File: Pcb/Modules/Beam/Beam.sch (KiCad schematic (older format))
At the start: 9 parts, among them J1 JACK_RJ45, Q1 Q_NMOS_GSD, U3 TSOP585xx

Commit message: Pcb layout for beam and projectile module
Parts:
- added C3: 10uF, Resistors_SMD:R_1206, symbol C_Small
- D1: value LD274 -> IR_LED; footprint LEDs:LED_D5.0mm -> LEDs:LED_D5.0mm_Horizontal_O1.27mm_Z15.0mm; symbol LD274 -> LED
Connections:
- net +3V3: now also C3.1
- net GND: now also C3.2
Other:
- moved on the sheet: C1
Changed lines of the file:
@@
 $EndDescr
 $Comp
-L LD274 D1
+L LED D1
 U 1 1 59CD43E5
-P 5450 2500
-F 0 "D1" H 5470 2570 50  0000 L CNN
-F 1 "LD274" H 5410 2390 50  0000 C CNN
-F 2 "LEDs:LED_D5.0mm" H 5450 2675 50  0001 C CNN
-F 3 "" H 5400 2500 50  0001 C CNN
-	1    5450 2500
+P 5450 2550
+F 0 "D1" H 5400 2650 50  0000 L CNN
+F 1 "IR_LED" H 5450 2400 50  0000 C CNN
+F 2 "LEDs:LED_D5.0mm_Horizontal_O1.27mm_Z15.0mm" H 5450 2725 50  0001 C CNN
+F 3 "" H 5400 2550 50  0001 C CNN
+	1    5450 2550
 	0    -1   -1   0
 $EndComp
@@
 L C_Small C1
 U 1 1 59D0EC2E
-P 3950 3450
-F 0 "C1" H 3960 3520 50  0000 L CNN
-F 1 "0.1uF" H 3960 3370 50  0000 L CNN
-F 2 "Resistors_SMD:R_0603" H 3950 3450 50  0001 C CNN
-F 3 "" H 3950 3450 50  0001 C CNN
-	1    3950 3450
-	1    0    0    -1
-$EndComp
-$Comp
-L +3.3V #PWR01
+P 3550 3450
+F 0 "C1" H 3560 3520 50  0000 L CNN
+F 1 "0.1uF" H 3560 3370 50  0000 L CNN
+F 2 "Resistors_SMD:R_0603" H 3550 3450 50  0001 C CNN
+F 3 "" H 3550 3450 50  0001 C CNN
+	1    3550 3450
+	1    0    0    -1
+$EndComp
+$Comp
+L +3.3V #PWR5
 U 1 1 59FCE3A1
 P 4500 2050
-F 0 "#PWR01" H 4500 1900 50  0001 C CNN
+F 0 "#PWR5" H 4500 1900 50  0001 C CNN
 F 1 "+3.3V" H 4500 2190 50  0000 C CNN
 F 2 "" H 4500 2050 50  0000 C CNN
@@
 $EndComp
 $Comp
-L GND #PWR02
+L GND #PWR6
 U 1 1 59FCE5A5
 P 4500 2850
-F 0 "#PWR02" H 4500 2600 50  0001 C CNN
+F 0 "#PWR6" H 4500 2600 50  0001 C CNN
 F 1 "GND" H 4500 2700 50  0000 C CNN
 F 2 "" H 4500 2850 50  0000 C CNN
@@
 $EndComp
 $Comp
-L GND #PWR03
+L GND #PWR10
 U 1 1 59FD6B4A
 P 6100 2100
-F 0 "#PWR03" H 6100 1850 50  0001 C CNN
+F 0 "#PWR10" H 6100 1850 50  0001 C CNN
 F 1 "GND" H 6100 1950 50  0000 C CNN
 F 2 "" H 6100 2100 50  0000 C CNN
@@
 $EndComp
 $Comp
-L +3.3V #PWR04
+L +3.3V #PWR9
 U 1 1 59FD6C0D
 P 5550 1300
-F 0 "#PWR04" H 5550 1150 50  0001 C CNN
+F 0 "#PWR9" H 5550 1150 50  0001 C CNN
 F 1 "+3.3V" H 5550 1440 50  0000 C CNN
 F 2 "" H 5550 1300 50  0000 C CNN
@@
 	6100 2000 6100 2100
 $Comp
-L GND #PWR05
+L GND #PWR11
 U 1 1 59FD6E29
 P 6450 2100
-F 0 "#PWR05" H 6450 1850 50  0001 C CNN
+F 0 "#PWR11" H 6450 1850 50  0001 C CNN
 F 1 "GND" H 6450 1950 50  0000 C CNN
 F 2 "" H 6450 2100 50  0000 C CNN
@@
 	6450 1850 6450 2100
 $Comp
-L GND #PWR06
+L GND #PWR2
 U 1 1 59FD6FDB
-P 3950 3600
-F 0 "#PWR06" H 3950 3350 50  0001 C CNN
-F 1 "GND" H 3950 3450 50  0000 C CNN
-F 2 "" H 3950 3600 50  0000 C CNN
-F 3 "" H 3950 3600 50  0000 C CNN
-	1    3950 3600
-	1    0    0    -1
-$EndComp
-$Comp
-L +3.3V #PWR07
+P 3550 3600
+F 0 "#PWR2" H 3550 3350 50  0001 C CNN
+F 1 "GND" H 3550 3450 50  0000 C CNN
+F 2 "" H 3550 3600 50  0000 C CNN
+F 3 "" H 3550 3600 50  0000 C CNN
+	1    3550 3600
+	1    0    0    -1
+$EndComp
+$Comp
+L +3.3V #PWR1
 U 1 1 59FD6FFE
-P 3950 3300
-F 0 "#PWR07" H 3950 3150 50  0001 C CNN
-F 1 "+3.3V" H 3950 3440 50  0000 C CNN
-F 2 "" H 3950 3300 50  0000 C CNN
-F 3 "" H 3950 3300 50  0000 C CNN
-	1    3950 3300
-	1    0    0    -1
-$EndComp
-Wire Wire Line
-	3950 3300 3950 3350
-Wire Wire Line
-	3950 3600 3950 3550
-$Comp
-L GND #PWR08
+P 3550 3300
+F 0 "#PWR1" H 3550 3150 50  0001 C CNN
+F 1 "+3.3V" H 3550 3440 50  0000 C CNN
+F 2 "" H 3550 3300 50  0000 C CNN
+F 3 "" H 3550 3300 50  0000 C CNN
+	1    3550 3300
+	1    0    0    -1
+$EndComp
+Wire Wire Line
+	3550 3300 3550 3350
+Wire Wire Line
+	3550 3600 3550 3550
+$Comp
+L GND #PWR8
 U 1 1 59FD7258
 P 5450 3250
-F 0 "#PWR08" H 5450 3000 50  0001 C CNN
+F 0 "#PWR8" H 5450 3000 50  0001 C CNN
 F 1 "GND" H 5450 3100 50  0000 C CNN
 F 2 "" H 5450 3250 50  0000 C CNN
@@
 $EndComp
 $Comp
-L +3.3V #PWR09
+L +3.3V #PWR7
 U 1 1 59FD72E3
 P 5450 2100
-F 0 "#PWR09" H 5450 1950 50  0001 C CNN
+F 0 "#PWR7" H 5450 1950 50  0001 C CNN
 F 1 "+3.3V" H 5450 2240 50  0000 C CNN
 F 2 "" H 5450 2100 50  0000 C CNN
@@
 NoConn ~ 4350 2600
 NoConn ~ 4350 2700
+$Comp
+L C_Small C3
+U 1 1 59FF8067
+P 4050 3450
+F 0 "C3" H 4060 3520 50  0000 L CNN
+F 1 "10uF" H 4060 3370 50  0000 L CNN
+F 2 "Resistors_SMD:R_1206" H 4050 3450 50  0001 C CNN
+F 3 "" H 4050 3450 50  0001 C CNN
+	1    4050 3450
+	1    0    0    -1
+$EndComp
+$Comp
+L GND #PWR4
+U 1 1 59FF806D
+P 4050 3600
+F 0 "#PWR4" H 4050 3350 50  0001 C CNN
+F 1 "GND" H 4050 3450 50  0000 C CNN
+F 2 "" H 4050 3600 50  0000 C CNN
+F 3 "" H 4050 3600 50  0000 C CNN
+	1    4050 3600
+	1    0    0    -1
+$EndComp
+$Comp
+L +3.3V #PWR3
+U 1 1 59FF8073
+P 4050 3300
+F 0 "#PWR3" H 4050 3150 50  0001 C CNN
+F 1 "+3.3V" H 4050 3440 50  0000 C CNN
+F 2 "" H 4050 3300 50  0000 C CNN
+F 3 "" H 4050 3300 50  0000 C CNN
+	1    4050 3300
+	1    0    0    -1
+$EndComp
+Wire Wire Line
+	4050 3300 4050 3350
+Wire Wire Line
+	4050 3600 4050 3550
 $EndSCHEMATC

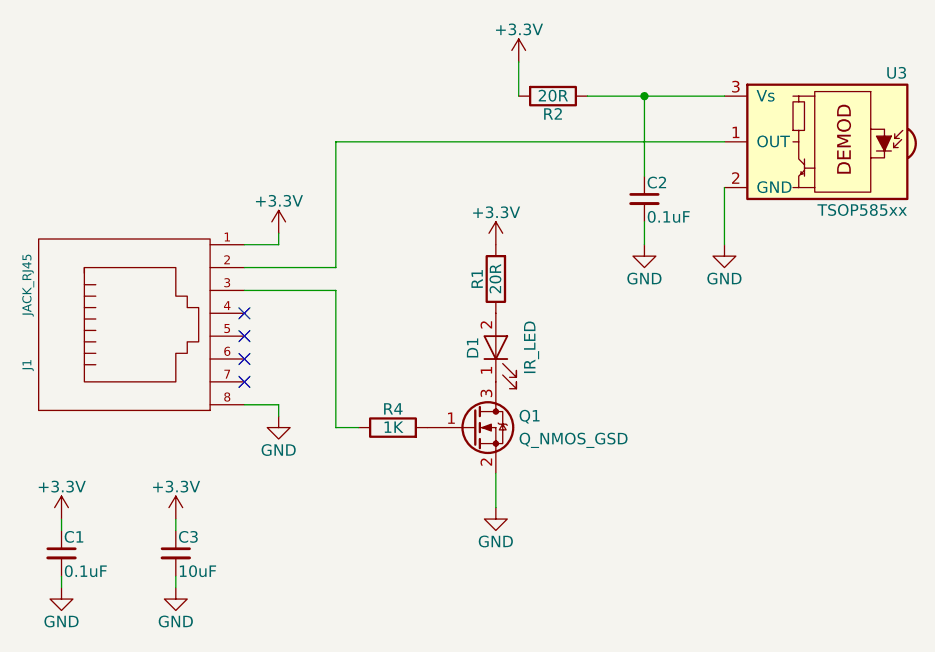
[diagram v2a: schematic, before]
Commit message: Update beam sensor to seperate the emitter and detector
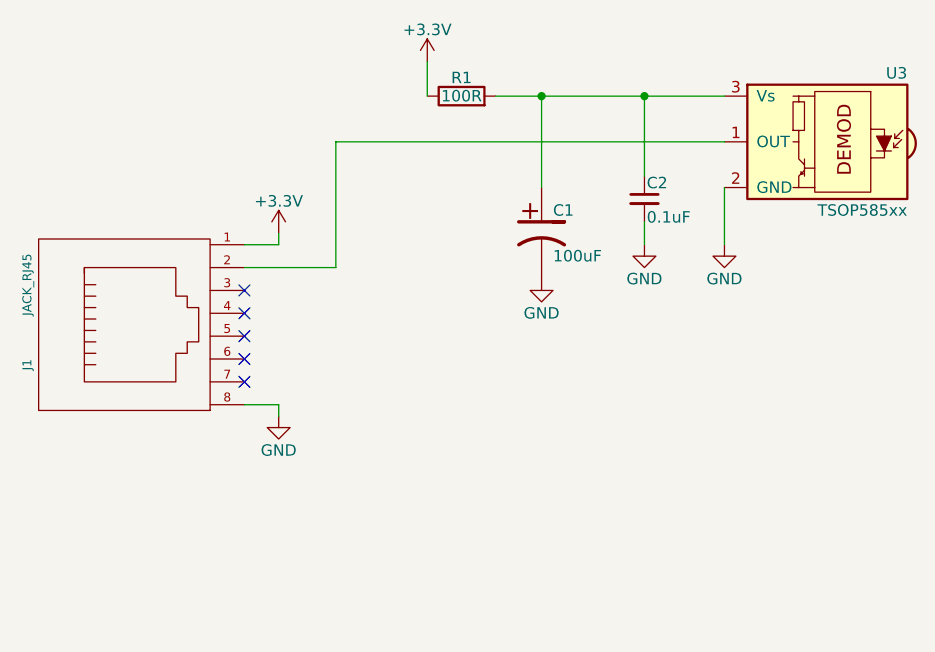
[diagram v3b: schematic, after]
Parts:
- removed C1: 0.1uF, Resistors_SMD:R_0603, symbol C_Small
- removed C3: 10uF, Resistors_SMD:R_1206, symbol C_Small
- removed D1: IR_LED, LEDs:LED_D5.0mm_Horizontal_O1.27mm_Z15.0mm, symbol LED
- removed Q1: Q_NMOS_GSD, TO_SOT_Packages_SMD:SOT-23, symbol Q_NMOS_GSD
- removed R2: 20R, Resistors_SMD:R_1206, symbol R
- removed R4: 1K, Resistors_SMD:R_0603, symbol R
- added C1: 100uF, CA6:c_elec_6.3x5.7, symbol CAP_ELEC
- R1: value 20R -> 100R; footprint Resistors_SMD:R_1206 -> Resistors_SMD:R_0603
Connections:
- net +3V3: now also R1.1; no longer R1.2
- net GND: now also C1.2
- net at C2.1, U3.3 (Vs): now also R1.2, C1.1
- no-connect marks 4 -> 5
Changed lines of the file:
@@
 $EndDescr
-$Comp
-L LED D1
-U 1 1 59CD43E5
-P 5450 2550
-F 0 "D1" H 5400 2650 50  0000 L CNN
-F 1 "IR_LED" H 5450 2400 50  0000 C CNN
-F 2 "LEDs:LED_D5.0mm_Horizontal_O1.27mm_Z15.0mm" H 5450 2725 50  0001 C CNN
-F 3 "" H 5400 2550 50  0001 C CNN
-	1    5450 2550
-	0    -1   -1   0
-$EndComp
 $Comp
 L TSOP585xx U3
@@
 $EndComp
 $Comp
-L R R4
-U 1 1 59D0E70C
-P 5000 2900
-F 0 "R4" V 5080 2900 50  0000 C CNN
-F 1 "1K" V 5000 2900 50  0000 C CNN
-F 2 "Resistors_SMD:R_0603" V 4930 2900 50  0001 C CNN
-F 3 "" H 5000 2900 50  0001 C CNN
-	1    5000 2900
-	0    -1   -1   0
-$EndComp
-$Comp
-L C_Small C1
-U 1 1 59D0EC2E
-P 3550 3450
-F 0 "C1" H 3560 3520 50  0000 L CNN
-F 1 "0.1uF" H 3560 3370 50  0000 L CNN
-F 2 "Resistors_SMD:R_0603" H 3550 3450 50  0001 C CNN
-F 3 "" H 3550 3450 50  0001 C CNN
-	1    3550 3450
-	1    0    0    -1
-$EndComp
-$Comp
-L +3.3V #PWR01
+L +3.3V #PWR1
 U 1 1 59FCE3A1
 P 4500 2050
-F 0 "#PWR01" H 4500 1900 50  0001 C CNN
+F 0 "#PWR1" H 4500 1900 50  0001 C CNN
 F 1 "+3.3V" H 4500 2190 50  0000 C CNN
 F 2 "" H 4500 2050 50  0000 C CNN
@@
 $EndComp
 $Comp
-L GND #PWR02
+L GND #PWR2
 U 1 1 59FCE5A5
 P 4500 2850
-F 0 "#PWR02" H 4500 2600 50  0001 C CNN
+F 0 "#PWR2" H 4500 2600 50  0001 C CNN
 F 1 "GND" H 4500 2700 50  0000 C CNN
 F 2 "" H 4500 2850 50  0000 C CNN
@@
 	1    4500 2850
 	1    0    0    -1
-$EndComp
-Wire Wire Line
-	4750 2900 4850 2900
-Wire Wire Line
-	5150 2900 5150 2900
-Wire Wire Line
-	5450 3100 5450 3250
-$Comp
-L R R2
-U 1 1 59CD46C4
-P 5700 1450
-F 0 "R2" V 5780 1450 50  0000 C CNN
-F 1 "20R" V 5700 1450 50  0000 C CNN
-F 2 "Resistors_SMD:R_1206" V 5630 1450 50  0001 C CNN
-F 3 "" H 5700 1450 50  0001 C CNN
-	1    5700 1450
-	0    1    1    0
 $EndComp
 $Comp
@@
 $EndComp
 $Comp
-L GND #PWR03
+L GND #PWR5
 U 1 1 59FD6B4A
 P 6100 2100
-F 0 "#PWR03" H 6100 1850 50  0001 C CNN
+F 0 "#PWR5" H 6100 1850 50  0001 C CNN
 F 1 "GND" H 6100 1950 50  0000 C CNN
 F 2 "" H 6100 2100 50  0000 C CNN
@@
 $EndComp
 $Comp
-L +3.3V #PWR04
+L +3.3V #PWR3
 U 1 1 59FD6C0D
-P 5550 1300
-F 0 "#PWR04" H 5550 1150 50  0001 C CNN
-F 1 "+3.3V" H 5550 1440 50  0000 C CNN
-F 2 "" H 5550 1300 50  0000 C CNN
-F 3 "" H 5550 1300 50  0000 C CNN
-	1    5550 1300
+P 5150 1300
+F 0 "#PWR3" H 5150 1150 50  0001 C CNN
+F 1 "+3.3V" H 5150 1440 50  0000 C CNN
+F 2 "" H 5150 1300 50  0000 C CNN
+F 3 "" H 5150 1300 50  0000 C CNN
+	1    5150 1300
 	1    0    0    -1
 $EndComp
 Wire Wire Line
-	5850 1450 6450 1450
+	5450 1450 6450 1450
 Wire Wire Line
-	5550 1300 5550 1450
+	5150 1300 5150 1450
 Wire Wire Line
 	6100 1450 6100 1800
@@
 	6100 2000 6100 2100
 $Comp
-L GND #PWR05
+L GND #PWR6
 U 1 1 59FD6E29
 P 6450 2100
-F 0 "#PWR05" H 6450 1850 50  0001 C CNN
+F 0 "#PWR6" H 6450 1850 50  0001 C CNN
 F 1 "GND" H 6450 1950 50  0000 C CNN
 F 2 "" H 6450 2100 50  0000 C CNN
@@
 Wire Wire Line
 	6450 1850 6450 2100
-$Comp
-L GND #PWR06
-U 1 1 59FD6FDB
-P 3550 3600
-F 0 "#PWR06" H 3550 3350 50  0001 C CNN
-F 1 "GND" H 3550 3450 50  0000 C CNN
-F 2 "" H 3550 3600 50  0000 C CNN
-F 3 "" H 3550 3600 50  0000 C CNN
-	1    3550 3600
-	1    0    0    -1
-$EndComp
-$Comp
-L +3.3V #PWR07
-U 1 1 59FD6FFE
-P 3550 3300
-F 0 "#PWR07" H 3550 3150 50  0001 C CNN
-F 1 "+3.3V" H 3550 3440 50  0000 C CNN
-F 2 "" H 3550 3300 50  0000 C CNN
-F 3 "" H 3550 3300 50  0000 C CNN
-	1    3550 3300
-	1    0    0    -1
-$EndComp
-Wire Wire Line
-	3550 3300 3550 3350
-Wire Wire Line
-	3550 3600 3550 3550
-$Comp
-L GND #PWR08
-U 1 1 59FD7258
-P 5450 3250
-F 0 "#PWR08" H 5450 3000 50  0001 C CNN
-F 1 "GND" H 5450 3100 50  0000 C CNN
-F 2 "" H 5450 3250 50  0000 C CNN
-F 3 "" H 5450 3250 50  0000 C CNN
-	1    5450 3250
-	1    0    0    -1
-$EndComp
-$Comp
-L +3.3V #PWR09
-U 1 1 59FD72E3
-P 5450 2100
-F 0 "#PWR09" H 5450 1950 50  0001 C CNN
-F 1 "+3.3V" H 5450 2240 50  0000 C CNN
-F 2 "" H 5450 2100 50  0000 C CNN
-F 3 "" H 5450 2100 50  0000 C CNN
-	1    5450 2100
-	1    0    0    -1
-$EndComp
 Wire Wire Line
 	6450 1650 4750 1650
@@
 	4750 1650 4750 2200
 Wire Wire Line
-	4750 2300 4750 2900
-$Comp
-L Q_NMOS_GSD Q1
-U 1 1 59FD80EC
-P 5350 2900
-F 0 "Q1" H 5550 2950 50  0000 L CNN
-F 1 "Q_NMOS_GSD" H 5550 2850 50  0000 L CNN
-F 2 "TO_SOT_Packages_SMD:SOT-23" H 5550 3000 50  0001 C CNN
-F 3 "" H 5350 2900 50  0000 C CNN
-	1    5350 2900
-	1    0    0    -1
-$EndComp
-Wire Wire Line
 	4750 2200 4350 2200
-Wire Wire Line
-	4750 2300 4350 2300
-$Comp
-L R R1
-U 1 1 59FD89F4
-P 5450 2250
-F 0 "R1" V 5530 2250 50  0000 C CNN
-F 1 "20R" V 5450 2250 50  0000 C CNN
-F 2 "Resistors_SMD:R_1206" V 5380 2250 50  0001 C CNN
-F 3 "" H 5450 2250 50  0001 C CNN
-	1    5450 2250
-	-1   0    0    1
-$EndComp
 $Comp
 L JACK_RJ45 J1
@@
 NoConn ~ 4350 2700
 $Comp
-L C_Small C3
-U 1 1 59FF8067
-P 4050 3450
-F 0 "C3" H 4060 3520 50  0000 L CNN
-F 1 "10uF" H 4060 3370 50  0000 L CNN
-F 2 "Resistors_SMD:R_1206" H 4050 3450 50  0001 C CNN
-F 3 "" H 4050 3450 50  0001 C CNN
-	1    4050 3450
-	1    0    0    -1
+L R R1
+U 1 1 5A21DC3C
+P 5300 1450
+F 0 "R1" V 5380 1450 50  0000 C CNN
+F 1 "100R" V 5300 1450 50  0000 C CNN
+F 2 "Resistors_SMD:R_0603" V 5230 1450 50  0001 C CNN
+F 3 "" H 5300 1450 50  0001 C CNN
+	1    5300 1450
+	0    -1   -1   0
 $EndComp
 $Comp
-L GND #PWR010
-U 1 1 59FF806D
-P 4050 3600
-F 0 "#PWR010" H 4050 3350 50  0001 C CNN
-F 1 "GND" H 4050 3450 50  0000 C CNN
-F 2 "" H 4050 3600 50  0000 C CNN
-F 3 "" H 4050 3600 50  0000 C CNN
-	1    4050 3600
-	1    0    0    -1
-$EndComp
-$Comp
-L +3.3V #PWR011
-U 1 1 59FF8073
-P 4050 3300
-F 0 "#PWR011" H 4050 3150 50  0001 C CNN
-F 1 "+3.3V" H 4050 3440 50  0000 C CNN
-F 2 "" H 4050 3300 50  0000 C CNN
-F 3 "" H 4050 3300 50  0000 C CNN
-	1    4050 3300
+L CAP_ELEC C1
+U 1 1 5A21DD7D
+P 5650 2050
+F 0 "C1" H 5700 2150 50  0000 L CNN
+F 1 "100uF" H 5700 1950 50  0000 L CNN
+F 2 "CA6:c_elec_6.3x5.7" H 5650 2050 60  0001 C CNN
+F 3 "" H 5650 2050 60  0000 C CNN
+	1    5650 2050
 	1    0    0    -1
 $EndComp
 Wire Wire Line
-	4050 3300 4050 3350
-Wire Wire Line
-	4050 3600 4050 3550
+	5650 1850 5650 1450
+Connection ~ 5650 1450
+$Comp
+L GND #PWR4
+U 1 1 5A21DE51
+P 5650 2250
+F 0 "#PWR4" H 5650 2000 50  0001 C CNN
+F 1 "GND" H 5650 2100 50  0000 C CNN
+F 2 "" H 5650 2250 50  0000 C CNN
+F 3 "" H 5650 2250 50  0000 C CNN
+	1    5650 2250
+	1    0    0    -1
+$EndComp
+NoConn ~ 4350 2300
 $EndSCHEMATC

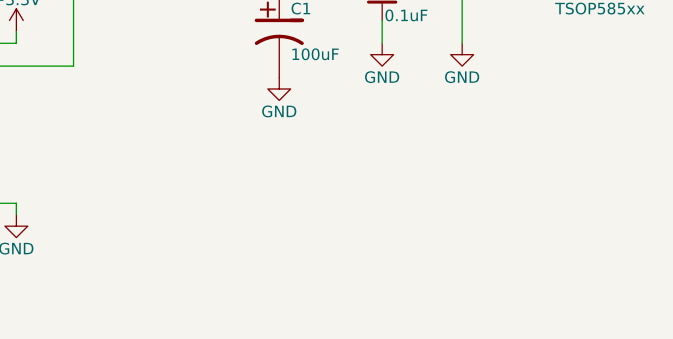
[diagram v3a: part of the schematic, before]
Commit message: Update module pcbs
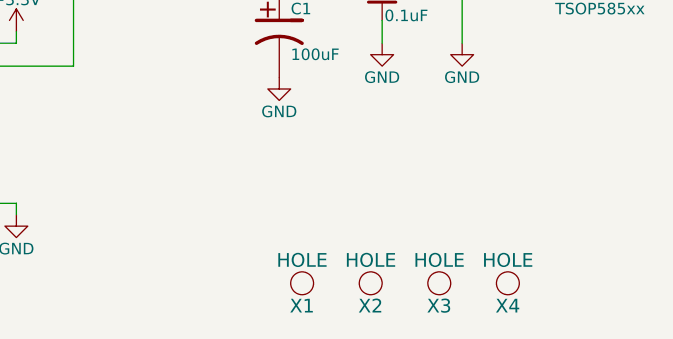
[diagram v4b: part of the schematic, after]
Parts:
- added X1, X2, X3, X4: HOLE, Mounting_Holes:MountingHole_2.5mm_Pad, symbol HOLE
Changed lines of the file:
@@
 $EndComp
 $Comp
-L +3.3V #PWR1
+L +3.3V #PWR01
 U 1 1 59FCE3A1
 P 4500 2050
-F 0 "#PWR1" H 4500 1900 50  0001 C CNN
+F 0 "#PWR01" H 4500 1900 50  0001 C CNN
 F 1 "+3.3V" H 4500 2190 50  0000 C CNN
 F 2 "" H 4500 2050 50  0000 C CNN
@@
 $EndComp
 $Comp
-L GND #PWR2
+L GND #PWR02
 U 1 1 59FCE5A5
 P 4500 2850
-F 0 "#PWR2" H 4500 2600 50  0001 C CNN
+F 0 "#PWR02" H 4500 2600 50  0001 C CNN
 F 1 "GND" H 4500 2700 50  0000 C CNN
 F 2 "" H 4500 2850 50  0000 C CNN
@@
 $EndComp
 $Comp
-L GND #PWR5
+L GND #PWR03
 U 1 1 59FD6B4A
 P 6100 2100
-F 0 "#PWR5" H 6100 1850 50  0001 C CNN
+F 0 "#PWR03" H 6100 1850 50  0001 C CNN
 F 1 "GND" H 6100 1950 50  0000 C CNN
 F 2 "" H 6100 2100 50  0000 C CNN
@@
 $EndComp
 $Comp
-L +3.3V #PWR3
+L +3.3V #PWR04
 U 1 1 59FD6C0D
 P 5150 1300
-F 0 "#PWR3" H 5150 1150 50  0001 C CNN
+F 0 "#PWR04" H 5150 1150 50  0001 C CNN
 F 1 "+3.3V" H 5150 1440 50  0000 C CNN
 F 2 "" H 5150 1300 50  0000 C CNN
@@
 	6100 2000 6100 2100
 $Comp
-L GND #PWR6
+L GND #PWR05
 U 1 1 59FD6E29
 P 6450 2100
-F 0 "#PWR6" H 6450 1850 50  0001 C CNN
+F 0 "#PWR05" H 6450 1850 50  0001 C CNN
 F 1 "GND" H 6450 1950 50  0000 C CNN
 F 2 "" H 6450 2100 50  0000 C CNN
@@
 Connection ~ 5650 1450
 $Comp
-L GND #PWR4
+L GND #PWR06
 U 1 1 5A21DE51
 P 5650 2250
-F 0 "#PWR4" H 5650 2000 50  0001 C CNN
+F 0 "#PWR06" H 5650 2000 50  0001 C CNN
 F 1 "GND" H 5650 2100 50  0000 C CNN
 F 2 "" H 5650 2250 50  0000 C CNN
@@
 $EndComp
 NoConn ~ 4350 2300
+$Comp
+L HOLE X1
+U 1 1 5A22D009
+P 5750 3150
+F 0 "X1" H 5750 3050 60  0000 C CNN
+F 1 "HOLE" H 5750 3250 60  0000 C CNN
+F 2 "Mounting_Holes:MountingHole_2.5mm_Pad" H 5750 3150 60  0001 C CNN
+F 3 "" H 5750 3150 60  0000 C CNN
+	1    5750 3150
+	1    0    0    -1
+$EndComp
+$Comp
+L HOLE X2
+U 1 1 5A22D141
+P 6050 3150
+F 0 "X2" H 6050 3050 60  0000 C CNN
+F 1 "HOLE" H 6050 3250 60  0000 C CNN
+F 2 "Mounting_Holes:MountingHole_2.5mm_Pad" H 6050 3150 60  0001 C CNN
+F 3 "" H 6050 3150 60  0000 C CNN
+	1    6050 3150
+	1    0    0    -1
+$EndComp
+$Comp
+L HOLE X3
+U 1 1 5A22D16C
+P 6350 3150
+F 0 "X3" H 6350 3050 60  0000 C CNN
+F 1 "HOLE" H 6350 3250 60  0000 C CNN
+F 2 "Mounting_Holes:MountingHole_2.5mm_Pad" H 6350 3150 60  0001 C CNN
+F 3 "" H 6350 3150 60  0000 C CNN
+	1    6350 3150
+	1    0    0    -1
+$EndComp
+$Comp
+L HOLE X4
+U 1 1 5A22D1A0
+P 6650 3150
+F 0 "X4" H 6650 3050 60  0000 C CNN
+F 1 "HOLE" H 6650 3250 60  0000 C CNN
+F 2 "Mounting_Holes:MountingHole_2.5mm_Pad" H 6650 3150 60  0001 C CNN
+F 3 "" H 6650 3150 60  0000 C CNN
+	1    6650 3150
+	1    0    0    -1
+$EndComp
 $EndSCHEMATC
